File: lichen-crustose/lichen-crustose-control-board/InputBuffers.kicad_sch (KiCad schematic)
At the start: 13 parts, among them J1 Thonkiconn_Mono_Audio_Jack, J2 Thonkiconn_Mono_Audio_Jack, J3 Thonkiconn_Mono_Audio_Jack, J4 Thonkiconn_Mono_Audio_Jack

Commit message: Updates Lichen symbols and footprints. Fixes to Crustose and Vactrol VCA. Adds 3D model of the RP2350 dual USB board.
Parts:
- J1, J2, J3, J4: now left out of the parts list
- R1, R2, R3, R5, R6, R7: JLCPCB ID C25803 -> (none); LCSC (none) -> C25803
- R4, R8: LCSC (none) -> C25803
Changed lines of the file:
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@@
 		(unit 1)
 		(exclude_from_sim no)
-		(in_bom yes)
+		(in_bom no)
 		(on_board yes)
 		(dnp no)
@@
 			)
 		)
-		(property "JLCPCB ID" "C25803"
+		(property "LCSC" "C25803"
 			(at 205.74 48.26 0)
 			(effects
@@
 			)
 		)
+		(property "LCSC" "C25803"
+			(at 190.5 142.24 0)
+			(effects
+				(font
+					(size 1.27 1.27)
+				)
+				(hide yes)
+			)
+		)
 		(pin "1"
 		)
@@
 			)
 		)
-		(property "JLCPCB ID" "C25803"
+		(property "LCSC" "C25803"
 			(at 190.5 82.55 0)
 			(effects
@@
 			)
 		)
+		(property "LCSC" "C25803"
+			(at 205.74 138.43 0)
+			(effects
+				(font
+					(size 1.27 1.27)
+				)
+				(hide yes)
+			)
+		)
 		(pin "1"
 		)
@@
 		(unit 1)
 		(exclude_from_sim no)
-		(in_bom yes)
+		(in_bom no)
 		(on_board yes)
 		(dnp no)
@@
 			)
 		)
-		(property "JLCPCB ID" "C25803"
+		(property "LCSC" "C25803"
 			(at 205.74 109.22 0)
 			(effects
@@
 		(unit 1)
 		(exclude_from_sim no)
-		(in_bom yes)
+		(in_bom no)
 		(on_board yes)
 		(dnp no)
@@
 			)
 		)
-		(property "JLCPCB ID" "C25803"
+		(property "LCSC" "C25803"
 			(at 205.74 78.74 0)
 			(effects
@@
 			)
 		)
-		(property "JLCPCB ID" "C25803"
+		(property "LCSC" "C25803"
 			(at 190.5 113.03 0)
 			(effects
@@
 			)
 		)
-		(property "JLCPCB ID" "C25803"
+		(property "LCSC" "C25803"
 			(at 190.5 52.07 0)
 			(effects
@@
 		(unit 1)
 		(exclude_from_sim no)
-		(in_bom yes)
-		(on_board yes)
-		(dnp no)
+		(in_bom no)
+		(on_board yes)
+		(dnp no)

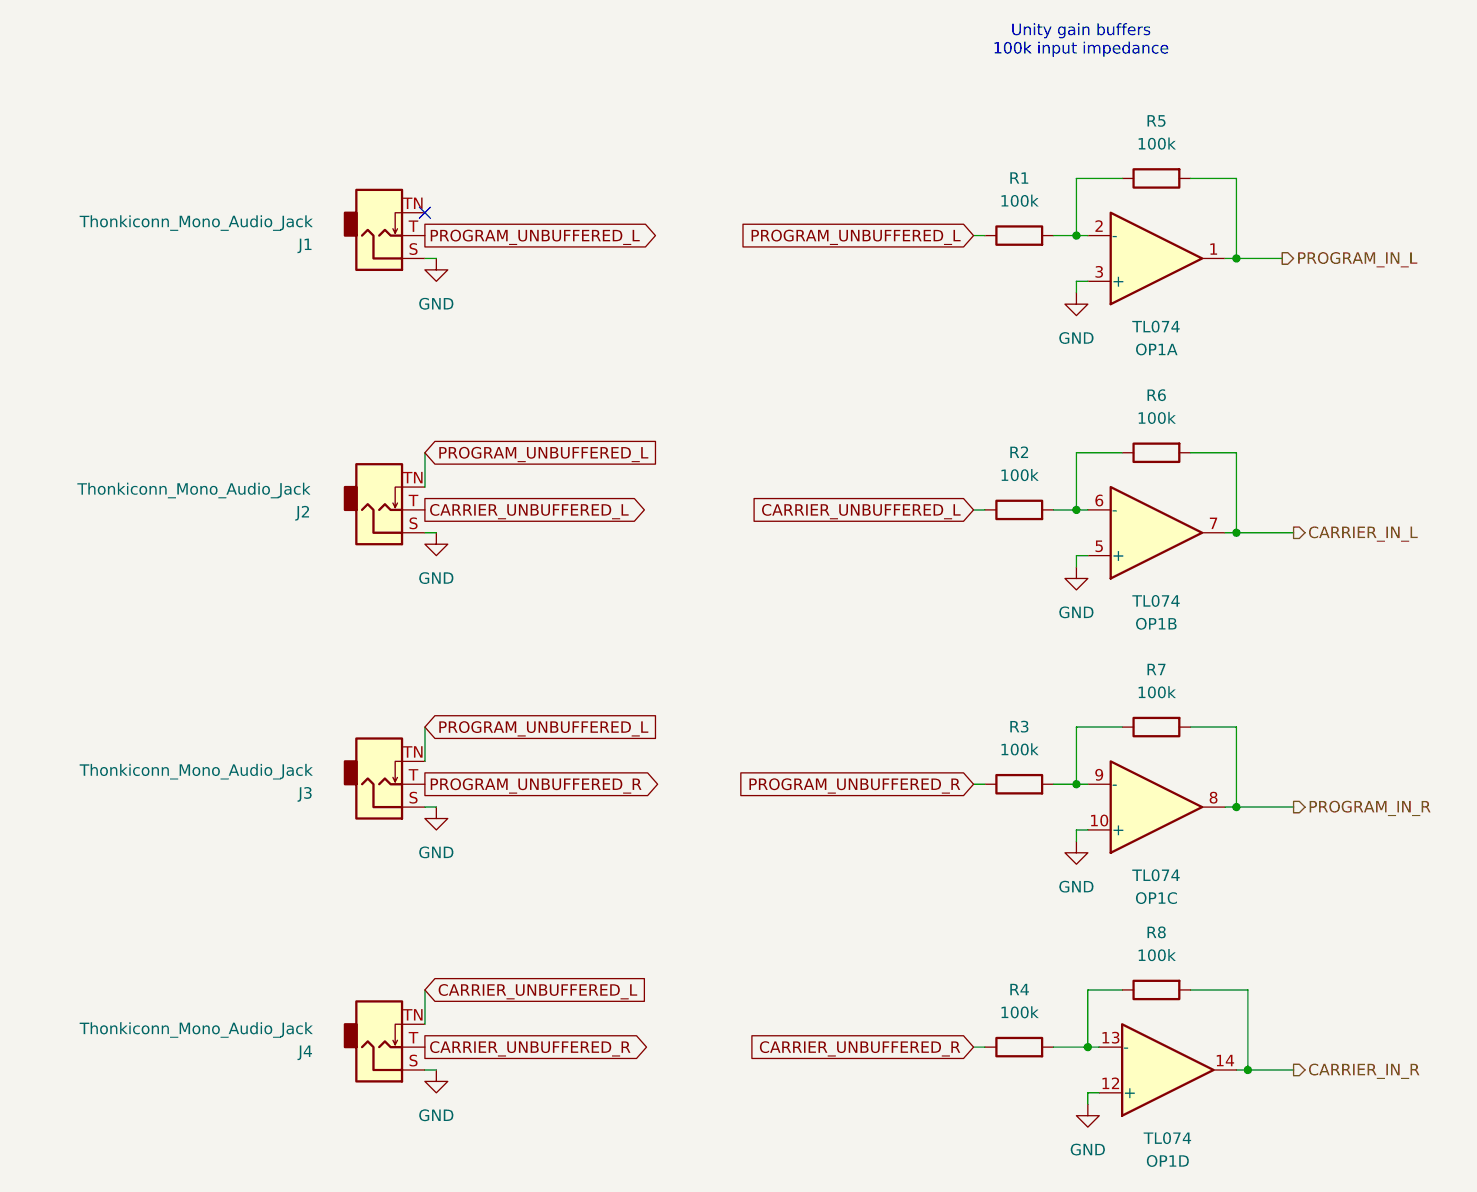
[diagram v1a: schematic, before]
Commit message: feat: Updates Crustose, Cladonia and YouMe Transformer. Adds Stereo Latencies.
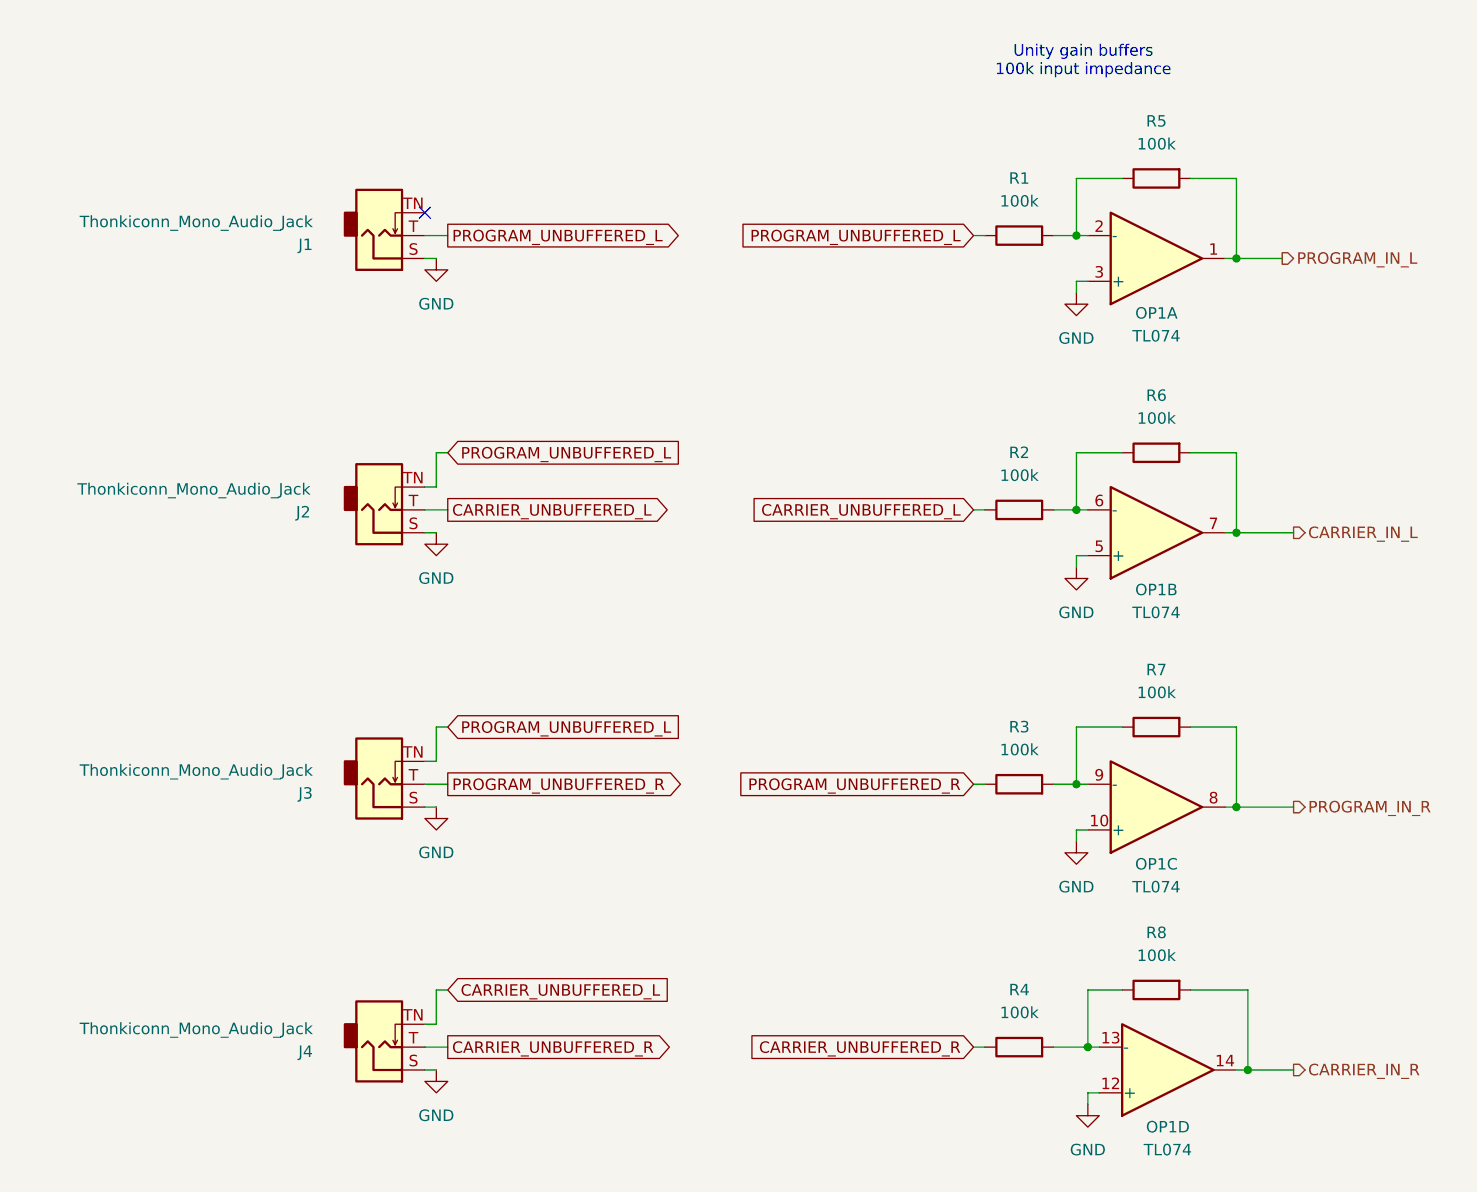
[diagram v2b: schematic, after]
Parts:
- OP1: symbol Amplifier_Operational:TL074 -> Lichen:TL074; LCSC (none) -> C6964; Manufacturer (none) -> Texas Instruments; Part Number (none) -> TL074IDR
- R1, R2, R3, R5, R6, R7, R8: value 100k_0603 -> 100K
- R4: value 100k_0603 -> 100K; JLCPCB ID C25803 -> (none)
